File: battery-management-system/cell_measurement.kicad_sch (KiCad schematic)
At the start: 0 parts

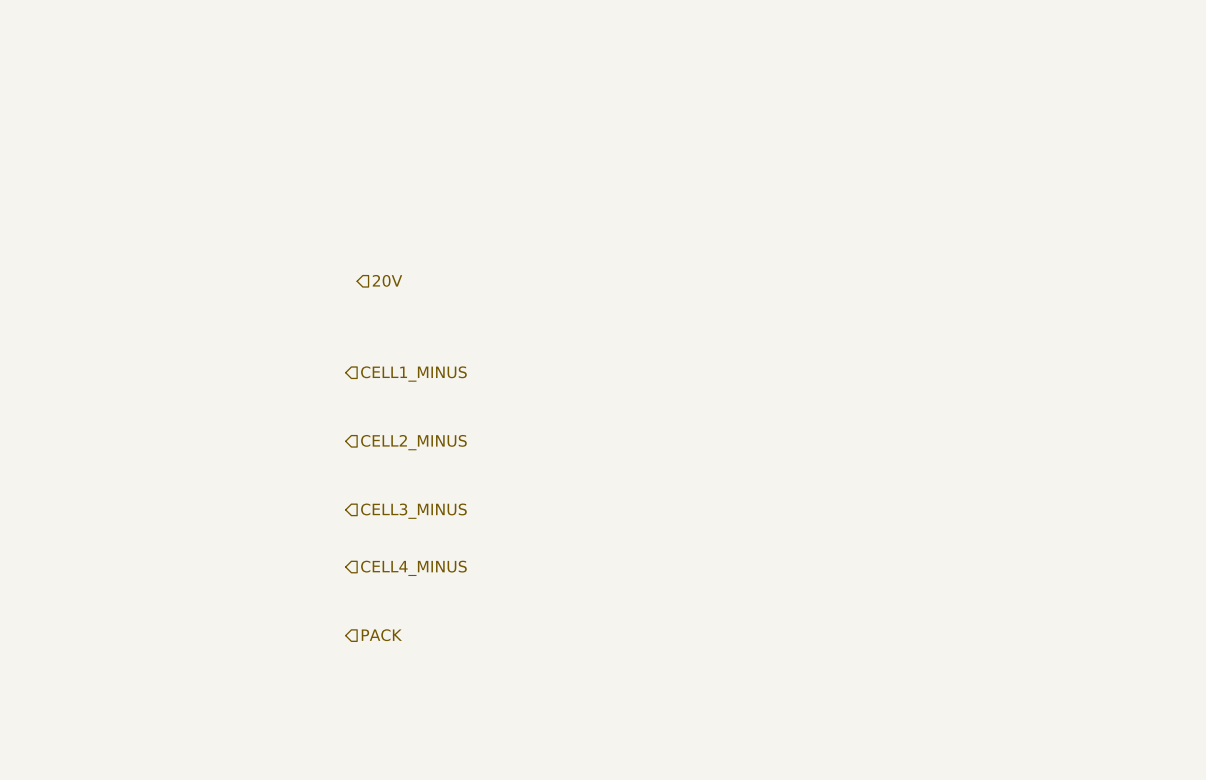
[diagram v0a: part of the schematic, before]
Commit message: implement interconnect
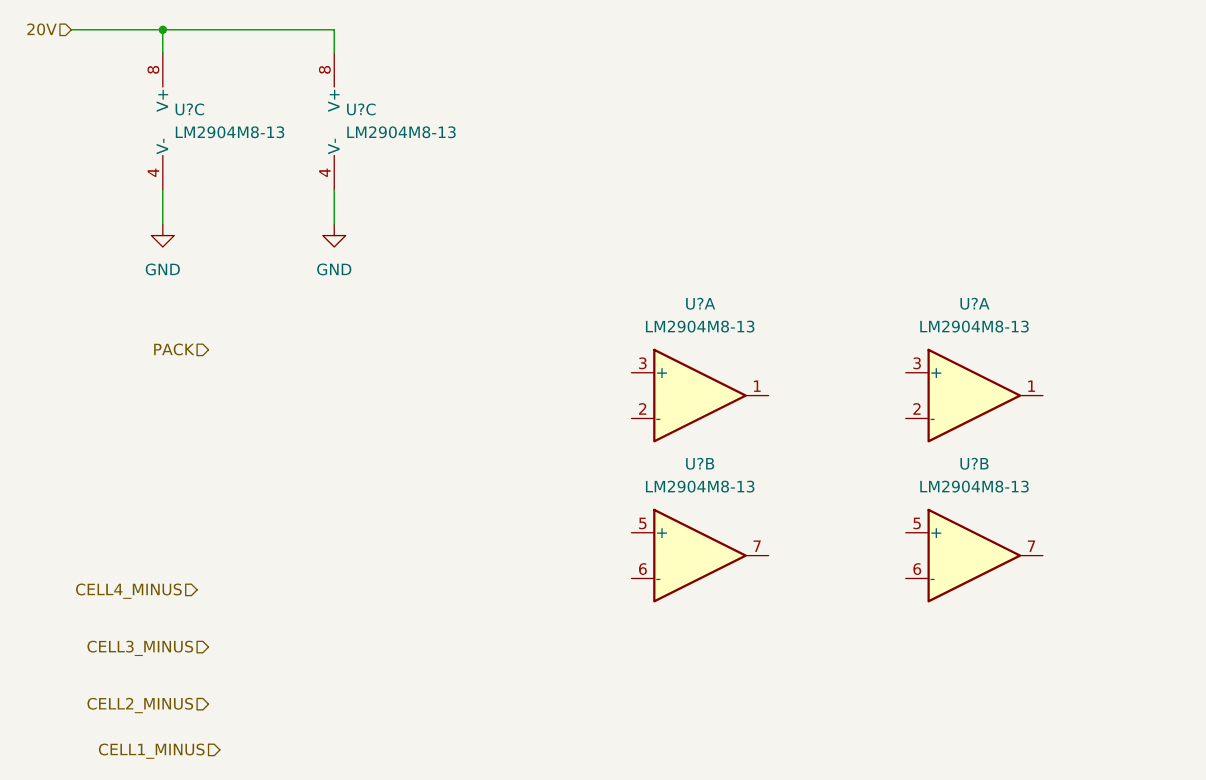
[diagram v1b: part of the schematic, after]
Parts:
- added U? (x6): LM2904M8-13, benediktibk:MSOP-8_3x3mm_P0.65mm, symbol benediktibk:LM2904M8-13
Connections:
- net 20V: now also U?.8 (V+), U?.8 (V+)
- new net GND: U?.4 (V-), U?.4 (V-)
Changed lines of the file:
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@@
 (kicad_sch (version 20211123) (generator eeschema)
   (paper "A4")
-  (hierarchical_label "CELL2_MINUS" (shape input) (at 55.88 60.96 0)
-    (effects (font (size 1.27 1.27)) (justify left))
+  (junction (at 35.56 15.24) (diameter 0) (color 0 0 0 0)
+  )
+  (wire (pts (xy 54.61 33.02) (xy 54.61 36.83))
+    (stroke (width 0) (type default) (color 0 0 0 0))
+  )
+  (wire (pts (xy 54.61 15.24) (xy 54.61 17.78))
+    (stroke (width 0) (type default) (color 0 0 0 0))
+  )
+  (wire (pts (xy 35.56 15.24) (xy 35.56 17.78))
+    (stroke (width 0) (type default) (color 0 0 0 0))
+  )
+  (wire (pts (xy 35.56 15.24) (xy 54.61 15.24))
+    (stroke (width 0) (type default) (color 0 0 0 0))
+  )
+  (wire (pts (xy 25.4 15.24) (xy 35.56 15.24))
+    (stroke (width 0) (type default) (color 0 0 0 0))
+  )
+  (wire (pts (xy 35.56 33.02) (xy 35.56 36.83))
+    (stroke (width 0) (type default) (color 0 0 0 0))
+  )
+  (hierarchical_label "CELL2_MINUS" (shape input) (at 40.64 90.17 180)
+    (effects (font (size 1.27 1.27)) (justify right))
   )
   (hierarchical_label "CELL4" (shape output) (at 172.72 60.96 0)
@@
     (effects (font (size 1.27 1.27)) (justify left))
   )
-  (hierarchical_label "CELL1_MINUS" (shape input) (at 55.88 53.34 0)
-    (effects (font (size 1.27 1.27)) (justify left))
-  )
-  (hierarchical_label "20V" (shape input) (at 57.15 43.18 0)
-    (effects (font (size 1.27 1.27)) (justify left))
-  )
-  (hierarchical_label "PACK" (shape input) (at 55.88 82.55 0)
-    (effects (font (size 1.27 1.27)) (justify left))
-  )
-  (hierarchical_label "CELL4_MINUS" (shape input) (at 55.88 74.93 0)
-    (effects (font (size 1.27 1.27)) (justify left))
-  )
-  (hierarchical_label "CELL3_MINUS" (shape input) (at 55.88 68.58 0)
-    (effects (font (size 1.27 1.27)) (justify left))
+  (hierarchical_label "CELL1_MINUS" (shape input) (at 41.91 95.25 180)
+    (effects (font (size 1.27 1.27)) (justify right))
+  )
+  (hierarchical_label "20V" (shape input) (at 25.4 15.24 180)
+    (effects (font (size 1.27 1.27)) (justify right))
+  )
+  (hierarchical_label "PACK" (shape input) (at 40.64 50.8 180)
+    (effects (font (size 1.27 1.27)) (justify right))
+  )
+  (hierarchical_label "CELL4_MINUS" (shape input) (at 39.37 77.47 180)
+    (effects (font (size 1.27 1.27)) (justify right))
+  )
+  (hierarchical_label "CELL3_MINUS" (shape input) (at 40.64 83.82 180)
+    (effects (font (size 1.27 1.27)) (justify right))
   )
   (hierarchical_label "CELL1" (shape output) (at 171.45 41.91 0)
     (effects (font (size 1.27 1.27)) (justify left))
   )
+  (symbol (lib_id "power:GND") (at 54.61 36.83 0) (unit 1)
+    (in_bom yes) (on_board yes) (fields_autoplaced)
+    (property "Reference" "#PWR?" (id 0) (at 54.61 43.18 0)
+      (effects (font (size 1.27 1.27)) hide)
+    )
+    (property "Value" "GND" (id 1) (at 54.61 41.91 0))
+    (property "Footprint" "" (id 2) (at 54.61 36.83 0)
+      (effects (font (size 1.27 1.27)) hide)
+    )
+    (property "Datasheet" "" (id 3) (at 54.61 36.83 0)
+      (effects (font (size 1.27 1.27)) hide)
+    )
+    (pin "1")
+  )
+  (symbol (lib_id "benediktibk:LM2904M8-13") (at 38.1 25.4 0) (unit 3)
+    (in_bom yes) (on_board yes) (fields_autoplaced)
+    (property "Reference" "U?" (id 0) (at 36.83 24.1299 0)
+      (effects (font (size 1.27 1.27)) (justify left))
+    )
+    (property "Value" "LM2904M8-13" (id 1) (at 36.83 26.6699 0)
+      (effects (font (size 1.27 1.27)) (justify left))
+    )
+    (property "Footprint" "benediktibk:MSOP-8_3x3mm_P0.65mm" (id 2) (at 38.1 25.4 0)
+      (effects (font (size 1.27 1.27)) hide)
+    )
+    (property "Datasheet" "" (id 3) (at 38.1 25.4 0)
+      (effects (font (size 1.27 1.27)) hide)
+    )
+    (property "RS order number" "133-3375" (id 4) (at 38.1 25.4 0)
+      (effects (font (size 1.27 1.27)) hide)
+    )
+    (pin "1")
+    (pin "2")
+    (pin "3")
+    (pin "5")
+    (pin "6")
+    (pin "7")
+    (pin "4")
+    (pin "8")
+  )
+  (symbol (lib_id "benediktibk:LM2904M8-13") (at 125.73 55.88 0) (unit 1)
+    (in_bom yes) (on_board yes) (fields_autoplaced)
+    (property "Reference" "U?" (id 0) (at 125.73 45.72 0))
+    (property "Value" "LM2904M8-13" (id 1) (at 125.73 48.26 0))
+    (property "Footprint" "benediktibk:MSOP-8_3x3mm_P0.65mm" (id 2) (at 125.73 55.88 0)
+      (effects (font (size 1.27 1.27)) hide)
+    )
+    (property "Datasheet" "" (id 3) (at 125.73 55.88 0)
+      (effects (font (size 1.27 1.27)) hide)
+    )
+    (property "RS order number" "133-3375" (id 4) (at 125.73 55.88 0)
+      (effects (font (size 1.27 1.27)) hide)
+    )
+    (pin "1")
+    (pin "2")
+    (pin "3")
+    (pin "5")
+    (pin "6")
+    (pin "7")
+    (pin "4")
+    (pin "8")
+  )
+  (symbol (lib_id "benediktibk:LM2904M8-13") (at 57.15 25.4 0) (unit 3)
+    (in_bom yes) (on_board yes) (fields_autoplaced)
+    (property "Reference" "U?" (id 0) (at 55.88 24.1299 0)
+      (effects (font (size 1.27 1.27)) (justify left))
+    )
+    (property "Value" "LM2904M8-13" (id 1) (at 55.88 26.6699 0)
+      (effects (font (size 1.27 1.27)) (justify left))
+    )
+    (property "Footprint" "benediktibk:MSOP-8_3x3mm_P0.65mm" (id 2) (at 57.15 25.4 0)
+      (effects (font (size 1.27 1.27)) hide)
+    )
+    (property "Datasheet" "" (id 3) (at 57.15 25.4 0)
+      (effects (font (size 1.27 1.27)) hide)
+    )
+    (property "RS order number" "133-3375" (id 4) (at 57.15 25.4 0)
+      (effects (font (size 1.27 1.27)) hide)
+    )
+    (pin "1")
+    (pin "2")
+    (pin "3")
+    (pin "5")
+    (pin "6")
+    (pin "7")
+    (pin "4")
+    (pin "8")
+  )
+  (symbol (lib_id "benediktibk:LM2904M8-13") (at 95.25 73.66 0) (unit 2)
+    (in_bom yes) (on_board yes) (fields_autoplaced)
+    (property "Reference" "U?" (id 0) (at 95.25 63.5 0))
+    (property "Value" "LM2904M8-13" (id 1) (at 95.25 66.04 0))
+    (property "Footprint" "benediktibk:MSOP-8_3x3mm_P0.65mm" (id 2) (at 95.25 73.66 0)
+      (effects (font (size 1.27 1.27)) hide)
+    )
+    (property "Datasheet" "" (id 3) (at 95.25 73.66 0)
+      (effects (font (size 1.27 1.27)) hide)
+    )
+    (property "RS order number" "133-3375" (id 4) (at 95.25 73.66 0)
+      (effects (font (size 1.27 1.27)) hide)
+    )
+    (pin "1")
+    (pin "2")
+    (pin "3")
+    (pin "5")
+    (pin "6")
+    (pin "7")
+    (pin "4")
+    (pin "8")
+  )
+  (symbol (lib_id "benediktibk:LM2904M8-13") (at 95.25 55.88 0) (unit 1)
+    (in_bom yes) (on_board yes) (fields_autoplaced)
+    (property "Reference" "U?" (id 0) (at 95.25 45.72 0))
+    (property "Value" "LM2904M8-13" (id 1) (at 95.25 48.26 0))
+    (property "Footprint" "benediktibk:MSOP-8_3x3mm_P0.65mm" (id 2) (at 95.25 55.88 0)
+      (effects (font (size 1.27 1.27)) hide)
+    )
+    (property "Datasheet" "" (id 3) (at 95.25 55.88 0)
+      (effects (font (size 1.27 1.27)) hide)
+    )
+    (property "RS order number" "133-3375" (id 4) (at 95.25 55.88 0)
+      (effects (font (size 1.27 1.27)) hide)
+    )
+    (pin "1")
+    (pin "2")
+    (pin "3")
+    (pin "5")
+    (pin "6")
+    (pin "7")
+    (pin "4")
+    (pin "8")
+  )
+  (symbol (lib_id "benediktibk:LM2904M8-13") (at 125.73 73.66 0) (unit 2)
+    (in_bom yes) (on_board yes) (fields_autoplaced)
+    (property "Reference" "U?" (id 0) (at 125.73 63.5 0))
+    (property "Value" "LM2904M8-13" (id 1) (at 125.73 66.04 0))
+    (property "Footprint" "benediktibk:MSOP-8_3x3mm_P0.65mm" (id 2) (at 125.73 73.66 0)
+      (effects (font (size 1.27 1.27)) hide)
+    )
+    (property "Datasheet" "" (id 3) (at 125.73 73.66 0)
+      (effects (font (size 1.27 1.27)) hide)
+    )
+    (property "RS order number" "133-3375" (id 4) (at 125.73 73.66 0)
+      (effects (font (size 1.27 1.27)) hide)
+    )
+    (pin "1")
+    (pin "2")
+    (pin "3")
+    (pin "5")
+    (pin "6")
+    (pin "7")
+    (pin "4")
+    (pin "8")
+  )
+  (symbol (lib_id "power:GND") (at 35.56 36.83 0) (unit 1)
+    (in_bom yes) (on_board yes) (fields_autoplaced)
+    (property "Reference" "#PWR?" (id 0) (at 35.56 43.18 0)
+      (effects (font (size 1.27 1.27)) hide)
+    )
+    (property "Value" "GND" (id 1) (at 35.56 41.91 0))
+    (property "Footprint" "" (id 2) (at 35.56 36.83 0)
+      (effects (font (size 1.27 1.27)) hide)
+    )
+    (property "Datasheet" "" (id 3) (at 35.56 36.83 0)
+      (effects (font (size 1.27 1.27)) hide)
+    )
+    (pin "1")
+  )
 )

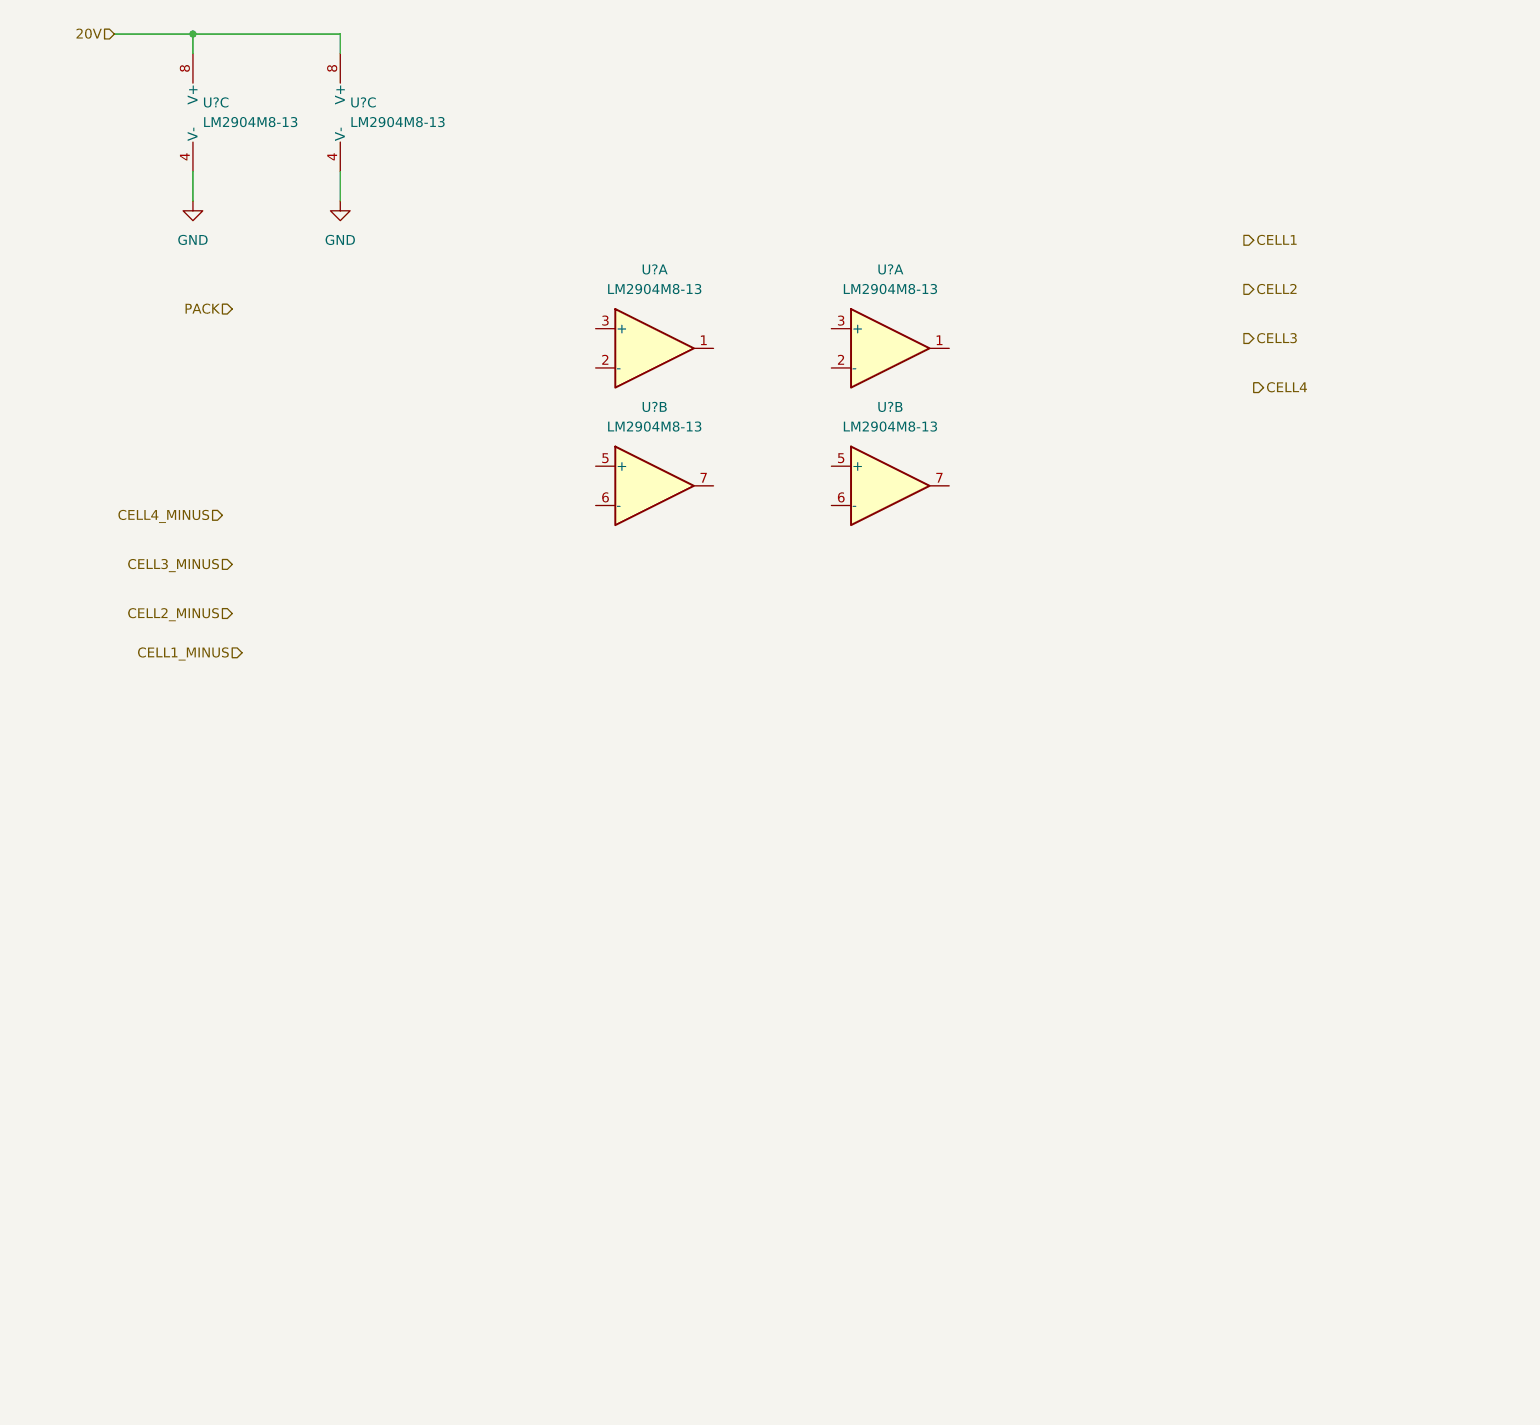
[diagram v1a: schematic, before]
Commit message: implement cell measurement
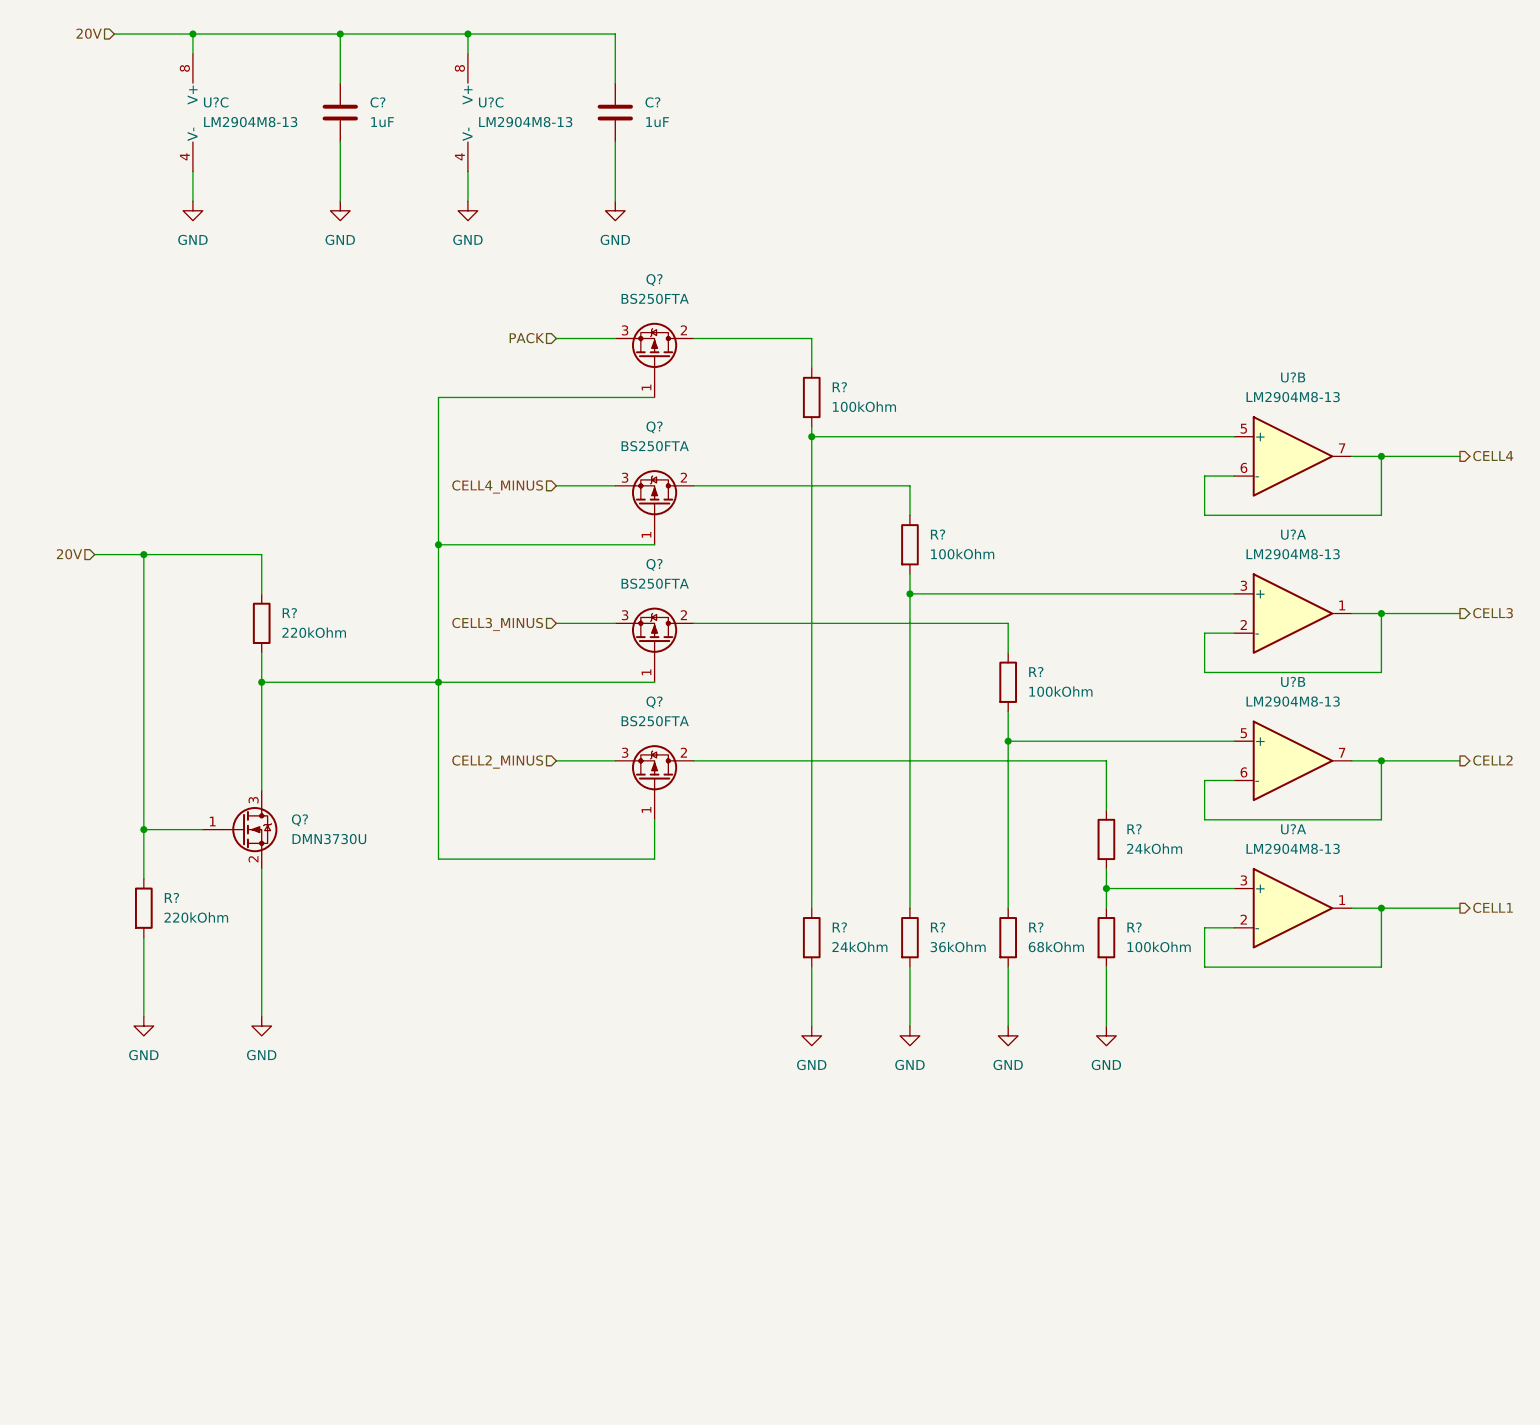
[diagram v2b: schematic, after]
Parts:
- added C? (x2): 1uF, benediktibk:C_0603_1608Metric_Pad1.08x0.95mm_HandSolder, symbol benediktibk:C_1uF_SMD_0603_50V_10%
- added Q? (x4): BS250FTA, benediktibk:SOT-23, symbol benediktibk:BS250FTA
- added Q?: DMN3730U, benediktibk:SOT-23, symbol benediktibk:DMN3730U
- added R? (x2): 24kOhm, benediktibk:R_0603_1608Metric_Pad0.98x0.95mm_HandSolder, symbol benediktibk:R_24kOhm_SMD_0603_100mW_1%
- added R? (x4): 100kOhm, benediktibk:R_0603_1608Metric_Pad0.98x0.95mm_HandSolder, symbol benediktibk:R_100kOhm_SMD_0603_100mW_1%
- added R? (x2): 220kOhm, benediktibk:R_0603_1608Metric_Pad0.98x0.95mm_HandSolder, symbol benediktibk:R_220kOhm_SMD_0603_100mW_1%
- added R?: 36kOhm, benediktibk:R_0603_1608Metric_Pad0.98x0.95mm_HandSolder, symbol benediktibk:R_36kOhm_SMD_0603_100mW_1%
- added R?: 68kOhm, benediktibk:R_0603_1608Metric_Pad0.98x0.95mm_HandSolder, symbol benediktibk:R_68kOhm_SMD_0603_100mW_1%
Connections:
- net 20V: now also C?.1, C?.1, Q?.1 (G), R?.1, R?.1
- net CELL1: now also U?.1, U?.2 (-)
- net CELL2: now also U?.6 (-), U?.7
- net CELL2_MINUS: now also Q?.3 (S)
- net CELL3: now also U?.1, U?.2 (-)
- net CELL3_MINUS: now also Q?.3 (S)
- net CELL4: now also U?.6 (-), U?.7
- net CELL4_MINUS: now also Q?.3 (S)
- net GND: now also C?.2, C?.2, Q?.2 (S), R?.2, R?.2, R?.2, R?.2, R?.2
- net PACK: now also Q?.3 (S)
- net at U?.3 (+): now also R?.1, R?.2 (x2)
- net at U?.5 (+): now also R?.1, R?.2 (x2)
- new net: Q?.1 (G), Q?.1 (G), Q?.1 (G), Q?.1 (G), Q?.3 (D), R?.2
- new net: Q?.2 (D), R?.1 (x4)
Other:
- moved on the sheet: U?A, U?B, U?C
